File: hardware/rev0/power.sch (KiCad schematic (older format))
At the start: 10 parts, among them U7 LD3985G30R, U8 LM3671

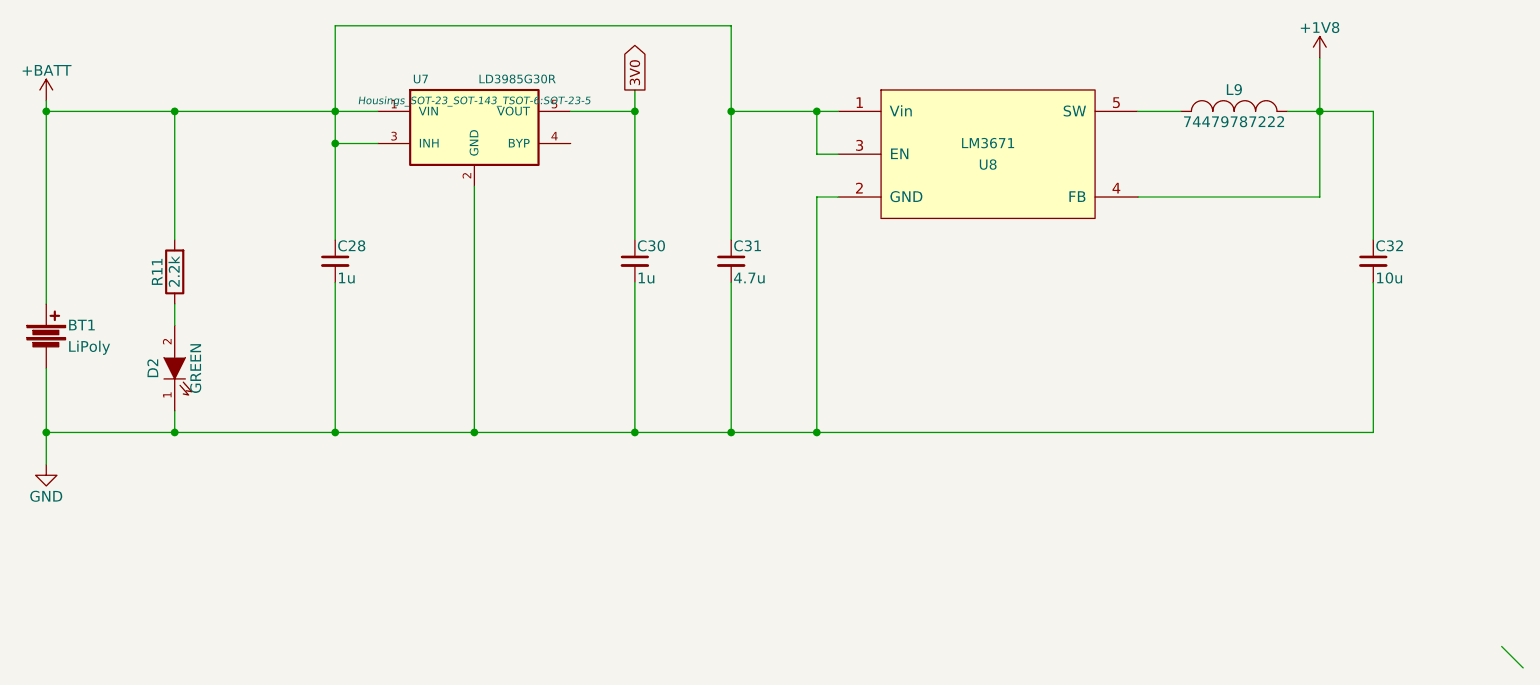
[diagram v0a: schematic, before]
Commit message: Replace TCXO with XTAL
Planned TCXO became obsolete and hard to source, high quality XTAL
should be good enough with possible temperature compensation in
software.
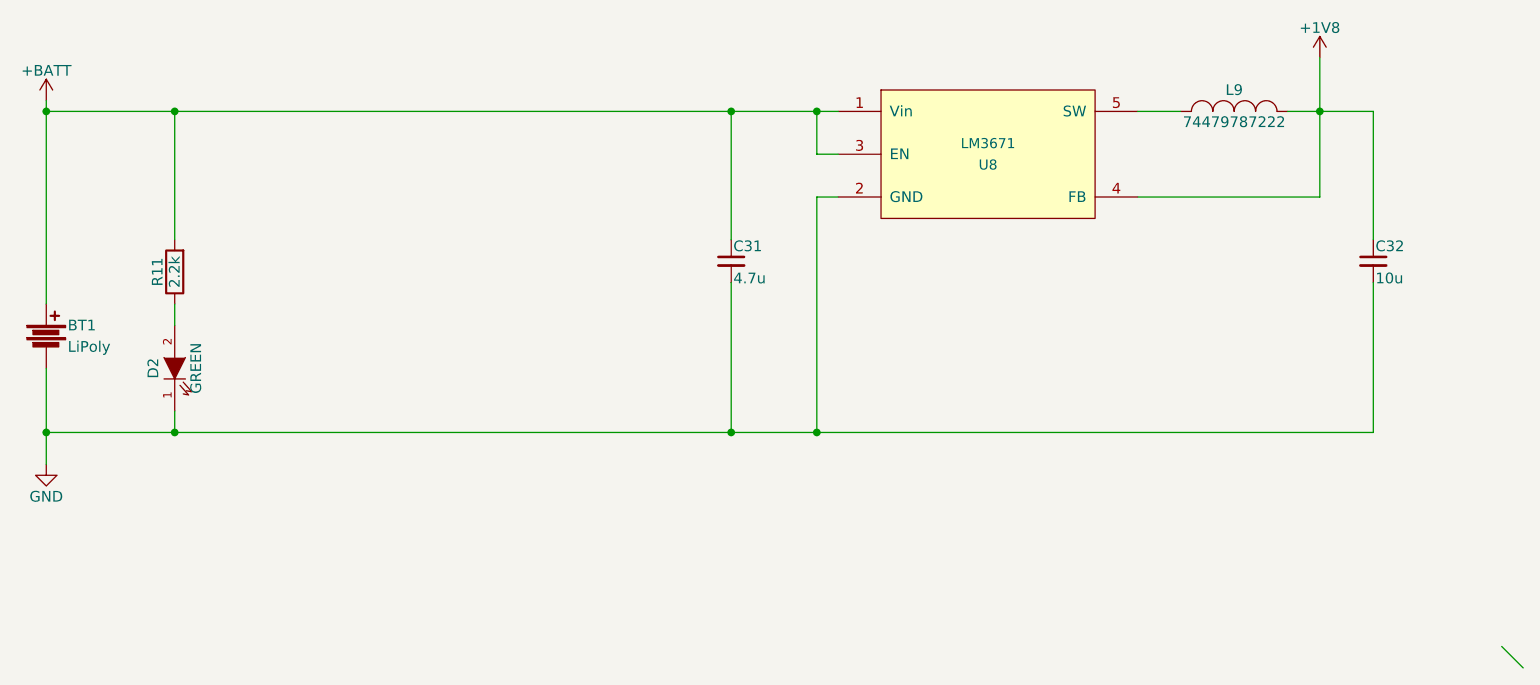
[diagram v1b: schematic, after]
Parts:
- removed C28, C30: 1u, Capacitors_SMD:C_0603, symbol C_Small
- removed U7: LD3985G30R, Housings_SOT-23_SOT-143_TSOT-6:SOT-23-5, symbol LD3985G30R
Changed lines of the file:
@@
 $EndComp
-$Comp
-L LD3985G30R U7
-U 1 1 563ADED4
-P 3800 1200
-F 0 "U7" H 3550 1400 40  0000 C CNN
-F 1 "LD3985G30R" H 4000 1400 40  0000 C CNN
-F 2 "Housings_SOT-23_SOT-143_TSOT-6:SOT-23-5" H 3800 1300 35  0000 C CIN
-F 3 "" H 3800 1200 60  0000 C CNN
-	1    3800 1200
-	1    0    0    -1
-$EndComp
-$Comp
-L C_Small C28
-U 1 1 563ADF70
-P 3150 1850
-F 0 "C28" H 3160 1920 50  0000 L CNN
-F 1 "1u" H 3160 1770 50  0000 L CNN
-F 2 "Capacitors_SMD:C_0603" H 3150 1850 60  0001 C CNN
-F 3 "" H 3150 1850 60  0000 C CNN
-	1    3150 1850
-	1    0    0    -1
-$EndComp
-$Comp
-L C_Small C30
-U 1 1 563AE19B
-P 4550 1850
-F 0 "C30" H 4560 1920 50  0000 L CNN
-F 1 "1u" H 4560 1770 50  0000 L CNN
-F 2 "Capacitors_SMD:C_0603" H 4550 1850 60  0001 C CNN
-F 3 "" H 4550 1850 60  0000 C CNN
-	1    4550 1850
-	1    0    0    -1
-$EndComp
-Text GLabel 4550 1050 1    47   Output ~ 0
-3V0
 $Comp
 L LM3671 U8
@@
 Wire Wire Line
 	5500 1550 5400 1550
-Connection ~ 4550 2650
 Wire Wire Line
 	5000 2650 5000 1950
@@
 Connection ~ 5000 1150
 Wire Wire Line
-	5000 1150 5500 1150
-Wire Wire Line
-	5000 750  5000 1750
-Wire Wire Line
-	3150 750  5000 750
-Connection ~ 4550 1150
-Wire Wire Line
-	4550 2650 4550 1950
-Wire Wire Line
-	4550 1150 4250 1150
-Wire Wire Line
-	4550 1050 4550 1750
-Connection ~ 3800 2650
-Connection ~ 3150 1300
-Wire Wire Line
-	3350 1300 3150 1300
-Connection ~ 3150 2650
-Wire Wire Line
-	3150 1950 3150 2650
-Connection ~ 3150 1150
-Wire Wire Line
-	3150 750  3150 1750
+	1800 1150 5500 1150
 Connection ~ 2400 2650
-Wire Wire Line
-	3800 2650 3800 1500
 Connection ~ 2400 1150
 Connection ~ 1800 1150
-Wire Wire Line
-	1800 1150 3350 1150
 Wire Wire Line
 	2400 1750 2400 1150
@@
 Wire Wire Line
 	2400 2650 2400 2550
-Wire Wire Line
-	1800 2650 8000 2650
 Wire Wire Line
 	1800 1100 1800 2050
@@
 Entry Wire Line
 	8600 3650 8700 3750
+Wire Wire Line
+	5000 1750 5000 1150
+Wire Wire Line
+	1800 2650 8000 2650
 $EndSCHEMATC

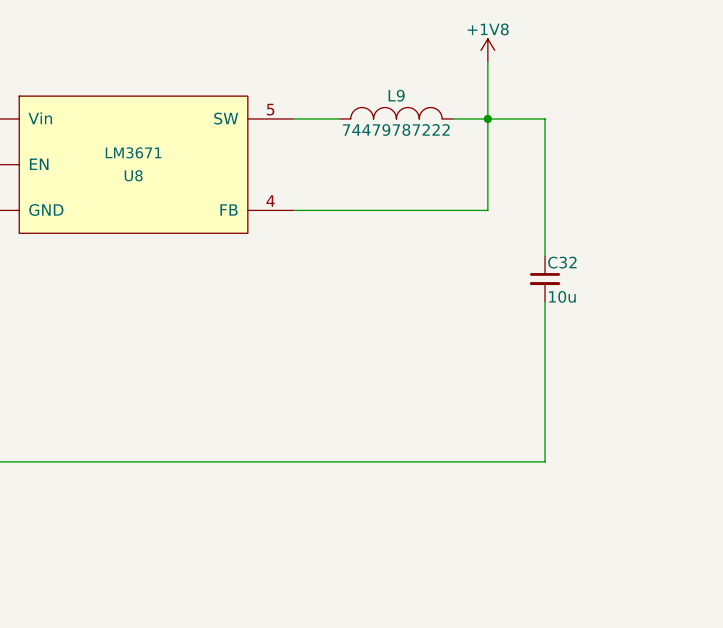
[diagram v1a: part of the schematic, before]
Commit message: Add FB network
Allow system to run off 2V if needed
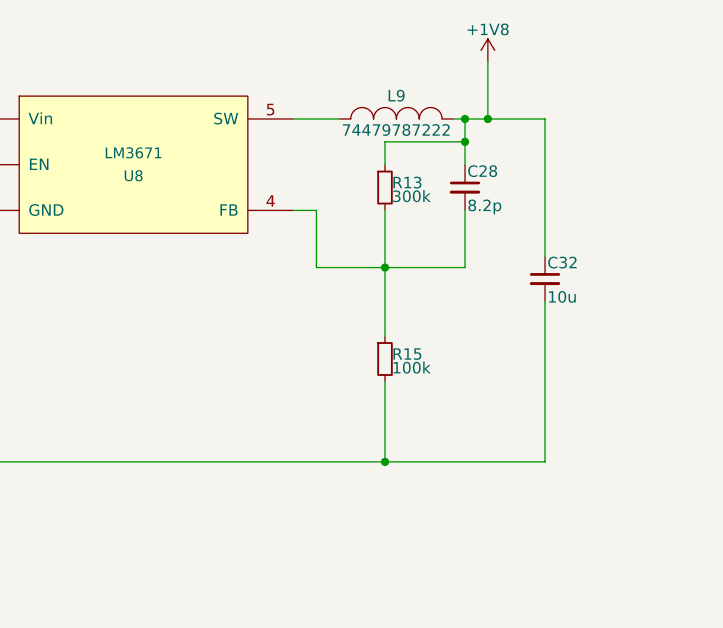
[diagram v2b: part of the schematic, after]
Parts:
- added C28: 8.2p, Capacitors_SMD:C_0402, symbol C_Small
- added R13: 300k, Resistors_SMD:R_0402, symbol R_Small
- added R15: 100k, Resistors_SMD:R_0402, symbol R_Small
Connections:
- net +1V8: now also C28.1, R13.1; no longer U8.4 (FB)
- net GND: now also R15.2
- new net: C28.2, R13.2, R15.1, U8.4 (FB)
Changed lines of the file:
@@
 	1    0    0    -1
 $EndComp
-Connection ~ 7750 1150
+$Comp
+L +1V8 #PWR020
+U 1 1 563AEAEA
+P 7750 900
+F 0 "#PWR020" H 7750 750 50  0001 C CNN
+F 1 "+1V8" H 7750 1040 50  0000 C CNN
+F 2 "" H 7750 900 60  0000 C CNN
+F 3 "" H 7750 900 60  0000 C CNN
+	1    7750 900
+	1    0    0    -1
+$EndComp
+Entry Wire Line
+	8600 3650 8700 3750
 Wire Wire Line
 	8000 1150 8000 1750
@@
 Wire Wire Line
 	7600 1150 8000 1150
-Wire Wire Line
-	7750 900  7750 1550
-Wire Wire Line
-	7750 1550 6900 1550
 Wire Wire Line
 	6900 1150 7100 1150
@@
 Wire Wire Line
 	1800 2350 1800 2800
-$Comp
-L +1V8 #PWR020
-U 1 1 563AEAEA
-P 7750 900
-F 0 "#PWR020" H 7750 750 50  0001 C CNN
-F 1 "+1V8" H 7750 1040 50  0000 C CNN
-F 2 "" H 7750 900 60  0000 C CNN
-F 3 "" H 7750 900 60  0000 C CNN
-	1    7750 900
-	1    0    0    -1
-$EndComp
-Entry Wire Line
-	8600 3650 8700 3750
 Wire Wire Line
 	5000 1750 5000 1150
 Wire Wire Line
 	1800 2650 8000 2650
+Wire Wire Line
+	7750 900  7750 1150
+Connection ~ 7750 1150
+$Comp
+L R_Small R13
+U 1 1 56ADFD0A
+P 7300 1450
+F 0 "R13" H 7330 1470 50  0000 L CNN
+F 1 "300k" H 7330 1410 50  0000 L CNN
+F 2 "Resistors_SMD:R_0402" H 7300 1450 50  0001 C CNN
+F 3 "" H 7300 1450 50  0000 C CNN
+	1    7300 1450
+	1    0    0    -1
+$EndComp
+$Comp
+L C_Small C28
+U 1 1 56ADFD7F
+P 7650 1450
+F 0 "C28" H 7660 1520 50  0000 L CNN
+F 1 "8.2p" H 7660 1370 50  0000 L CNN
+F 2 "Capacitors_SMD:C_0402" H 7650 1450 50  0001 C CNN
+F 3 "" H 7650 1450 50  0000 C CNN
+	1    7650 1450
+	1    0    0    -1
+$EndComp
+Wire Wire Line
+	7300 1350 7300 1250
+Wire Wire Line
+	7300 1250 7650 1250
+Wire Wire Line
+	7650 1150 7650 1350
+Connection ~ 7650 1150
+Connection ~ 7650 1250
+Wire Wire Line
+	6900 1550 7000 1550
+Wire Wire Line
+	7000 1550 7000 1800
+Wire Wire Line
+	7000 1800 7650 1800
+Wire Wire Line
+	7650 1800 7650 1550
+Wire Wire Line
+	7300 1550 7300 2100
+Connection ~ 7300 1800
+$Comp
+L R_Small R15
+U 1 1 56ADFF8A
+P 7300 2200
+F 0 "R15" H 7330 2220 50  0000 L CNN
+F 1 "100k" H 7330 2160 50  0000 L CNN
+F 2 "Resistors_SMD:R_0402" H 7300 2200 50  0001 C CNN
+F 3 "" H 7300 2200 50  0000 C CNN
+	1    7300 2200
+	1    0    0    -1
+$EndComp
+Wire Wire Line
+	7300 2650 7300 2300
+Connection ~ 7300 2650
 $EndSCHEMATC
